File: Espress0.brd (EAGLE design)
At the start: 36.8 x 39.4 mm, 41 parts, among them CN1 4U#20329, Q2 reset, U1 AP2112K-3.3, U2 2MB Flash, U3 MCP73831T-2ACI/OT

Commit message: Add files via upload
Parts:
- moved PWR 0.38 mm to (29.7, 3.94)
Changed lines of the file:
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@@
 <text x="4.699" y="27.305" size="0.6096" layer="121" font="vector" rot="R90">SDA</text>
 <text x="7.239" y="25.019" size="0.6096" layer="121" font="vector">SCL</text>
-<text x="6.35" y="35.56" size="1.6764" layer="121" font="fixed">Espress0</text>
+<text x="6.223" y="35.179" size="1.6764" layer="121" font="fixed">Espress0</text>
 <text x="30.48" y="36.195" size="0.6096" layer="122" rot="MR0">Based on Trinket m0 by Adafruit Industries.</text>
-<text x="6.35" y="33.782" size="0.6096" layer="121">04/2018 - v0.2</text>
+<text x="31.496" y="1.143" size="0.6096" layer="122" rot="MR0">04/2018 - v0.2</text>
 <text x="5.08" y="1.016" size="0.6096" layer="121">www.timothygarcia.ca</text>
 <text x="1.016" y="25.908" size="0.6096" layer="121" font="vector" rot="R90">pa05</text>
@@
 <text x="35.56" y="31.75" size="0.6096" layer="121" font="vector" rot="R270">VBAT</text>
 <text x="35.56" y="28.702" size="0.6096" layer="121" font="vector" rot="R270">GND</text>
-<text x="30.48" y="36.195" size="0.6096" layer="121" rot="R180">a trinket m0 haxpress board</text>
+<text x="30.48" y="36.068" size="0.6096" layer="121" rot="R180">a trinket m0 haxpress board</text>
 <text x="30.48" y="37.592" size="0.6096" layer="122" rot="MR0.6">Designed for CircuitPython</text>
 <text x="30.48" y="34.798" size="0.6096" layer="122" rot="MR0">Open Source Hardware</text>
@@
 <attribute name="NAME" x="20.858" y="32.242" size="0.4064" layer="25" ratio="18"/>
 </element>
-<element name="PWR" library="microbuilder" package="CHIPLED_0603_NOOUTLINE" value="green" x="29.337" y="3.937" smashed="yes" rot="R180">
-<attribute name="NAME" x="28.702" y="1.524" size="0.8128" layer="25" ratio="18"/>
-<attribute name="VALUE" x="28.829" y="5.461" size="0.4064" layer="121" ratio="10"/>
+<element name="PWR" library="microbuilder" package="CHIPLED_0603_NOOUTLINE" value="green" x="29.718" y="3.937" smashed="yes" rot="R180">
+<attribute name="NAME" x="31.369" y="6.35" size="0.8128" layer="25" ratio="18" rot="R180"/>
+<attribute name="VALUE" x="28.702" y="2.667" size="0.4064" layer="121" ratio="10" rot="R90"/>
 </element>
 <element name="Q2" library="microbuilder" package="BTN_KMR2_4.6X2.8" value="reset" x="33.401" y="15.24" smashed="yes" rot="R270">
@@
 </element>
 <element name="R4" library="microbuilder" package="0603-NO" value="10K" x="27.305" y="3.81" smashed="yes" rot="R270">
-<attribute name="NAME" x="26.289" y="3.048" size="0.6096" layer="121" font="vector" ratio="18" rot="R180"/>
-<attribute name="VALUE" x="26.289" y="2.159" size="0.4064" layer="121" font="vector" ratio="10" rot="R180"/>
+<attribute name="NAME" x="25.781" y="3.302" size="0.6096" layer="121" font="vector" ratio="18" rot="R270"/>
+<attribute name="VALUE" x="27.686" y="5.969" size="0.4064" layer="121" font="vector" ratio="10" rot="R180"/>
 </element>
 <element name="R5" library="microbuilder" package="0603-NO" value="10K" x="7.62" y="15.24" smashed="yes" rot="R180">
@@
 </element>
 <element name="SWC" library="testpad" package="B1,27" value="TPB1,27" x="27.559" y="20.574" smashed="yes" rot="MR0">
-<attribute name="NAME" x="28.575" y="21.082" size="0.4064" layer="26" ratio="10" rot="MR180"/>
+<attribute name="NAME" x="28.321" y="21.463" size="0.4064" layer="26" ratio="10" rot="MR180"/>
 <attribute name="TP_SIGNAL_NAME" value="" x="28.194" y="18.669" size="1" layer="38" rot="MR0"/>
 <attribute name="VALUE" x="28.194" y="19.812" size="0.0254" layer="28" rot="MR0"/>
 </element>
 <element name="SWD" library="testpad" package="B1,27" value="TPB1,27" x="25.273" y="22.733" smashed="yes" rot="MR0">
-<attribute name="NAME" x="25.273" y="21.336" size="0.4064" layer="26" ratio="10" rot="MR180"/>
+<attribute name="NAME" x="24.765" y="24.511" size="0.4064" layer="26" ratio="10" rot="MR180"/>
 <attribute name="TP_SIGNAL_NAME" value="" x="25.908" y="20.828" size="1" layer="38" rot="MR0"/>
 <attribute name="VALUE" x="25.908" y="21.971" size="0.0254" layer="28" rot="MR0"/>
@@
 </element>
 <element name="U1" library="microbuilder" package="SOT23-5" value="AP2112K-3.3" x="27.559" y="17.018" smashed="yes" rot="R90">
-<attribute name="NAME" x="29.464" y="18.488" size="0.8128" layer="25" ratio="18" rot="R90"/>
-<attribute name="VALUE" x="29.845" y="19.612" size="0.4064" layer="121" ratio="10" rot="R270"/>
+<attribute name="NAME" x="28.775" y="18.796" size="0.6096" layer="25" ratio="18"/>
+<attribute name="VALUE" x="29.845" y="18.342" size="0.3048" layer="121" ratio="10" rot="R270"/>
 </element>
 <element name="U2" library="microbuilder" package="SOIC8_208MIL" value="2MB Flash" x="11.049" y="10.16" smashed="yes" rot="R90">
@@
 <wire x1="29.4350875" y1="19.891" x2="30.548" y2="19.891" width="0.3048" layer="1"/>
 <wire x1="27.81315" y1="20.32" x2="29.0060875" y2="20.32" width="0.3048" layer="1"/>
-<wire x1="31.389" y1="19.05" x2="31.389" y2="9.799" width="0.3048" layer="1"/>
+<wire x1="31.389" y1="19.05" x2="31.389" y2="12.7" width="0.3048" layer="1"/>
+<wire x1="31.389" y1="12.7" x2="31.389" y2="9.799" width="0.3048" layer="1"/>
 <wire x1="31.389" y1="9.799" x2="30.48" y2="8.89" width="0.3048" layer="1"/>
 <wire x1="30.48" y1="8.89" x2="26.67" y2="8.89" width="0.3048" layer="1"/>
@@
 <wire x1="30.353" y1="28.736" x2="30.353" y2="29.845" width="0.3048" layer="1"/>
 <wire x1="30.353" y1="29.845" x2="30.607" y2="30.099" width="0.3048" layer="1"/>
-<wire x1="21.844" y1="6.985" x2="24.384" y2="6.985" width="0.4064" layer="1"/>
+<wire x1="21.844" y1="6.985" x2="22.86" y2="6.985" width="0.4064" layer="1"/>
+<wire x1="22.86" y1="6.985" x2="24.384" y2="6.985" width="0.4064" layer="1"/>
 <wire x1="25.146" y1="7.747" x2="25.146" y2="10.922" width="0.4064" layer="1"/>
 <wire x1="24.384" y1="6.985" x2="25.146" y2="7.747" width="0.4064" layer="1"/>
@@
 <contactref element="R4" pad="1"/>
 <contactref element="PWR" pad="A"/>
-<wire x1="29.337" y1="4.687" x2="27.332" y2="4.687" width="0.3048" layer="1"/>
+<wire x1="29.718" y1="4.687" x2="27.332" y2="4.687" width="0.3048" layer="1"/>
 <wire x1="27.332" y1="4.687" x2="27.305" y2="4.66" width="0.3048" layer="1"/>
 </signal>
@@
 <wire x1="33.3558" y1="12.61375" x2="33.02" y2="12.27795" width="0.3048" layer="1"/>
 <wire x1="31.8462" y1="15.27585" x2="33.3558" y2="13.76625" width="0.3048" layer="1"/>
-<wire x1="31.8462" y1="27.8312" x2="31.8462" y2="15.27585" width="0.3048" layer="1"/>
+<wire x1="31.8462" y1="27.8312" x2="31.8462" y2="21.59" width="0.3048" layer="1"/>
+<wire x1="31.8462" y1="21.59" x2="31.8462" y2="15.27585" width="0.3048" layer="1"/>
 <wire x1="31.8462" y1="27.8312" x2="29.62675" y2="27.8312" width="0.3048" layer="1"/>
 <wire x1="27.8431" y1="25.08" x2="28.636" y2="25.08" width="0.3048" layer="1"/>
@@
 <contactref element="U1" pad="3"/>
 <wire x1="28.4345" y1="10.922" x2="29.7315" y2="10.922" width="0.4064" layer="1"/>
-<wire x1="29.7315" y1="10.922" x2="29.7315" y2="13.7955" width="0.4064" layer="1"/>
+<wire x1="29.7315" y1="10.922" x2="29.7315" y2="12.7" width="0.4064" layer="1"/>
+<wire x1="29.7315" y1="12.7" x2="29.7315" y2="13.7955" width="0.4064" layer="1"/>
 <wire x1="29.7315" y1="13.7955" x2="29.779" y2="13.843" width="0.4064" layer="1"/>
 <wire x1="28.11180625" y1="16.3874" x2="27.9035" y2="16.59570625" width="0.4064" layer="1"/>
@@
 <wire x1="23.749" y1="8.128" x2="25.781" y2="6.096" width="0.3048" layer="16"/>
 <wire x1="6.35" y1="15.24" x2="6.77" y2="15.24" width="0.4064" layer="1"/>
-<wire x1="24.384" y1="16.168" x2="26.1589" y2="16.168" width="0.4064" layer="1"/>
+<wire x1="24.384" y1="16.168" x2="25.4" y2="16.168" width="0.4064" layer="1"/>
+<wire x1="25.4" y1="16.168" x2="26.1589" y2="16.168" width="0.4064" layer="1"/>
 <wire x1="26.1589" y1="16.168" x2="26.2589" y2="16.068" width="0.4064" layer="1"/>
 <via x="10.922" y="18.288" extent="1-16" drill="0.35"/>

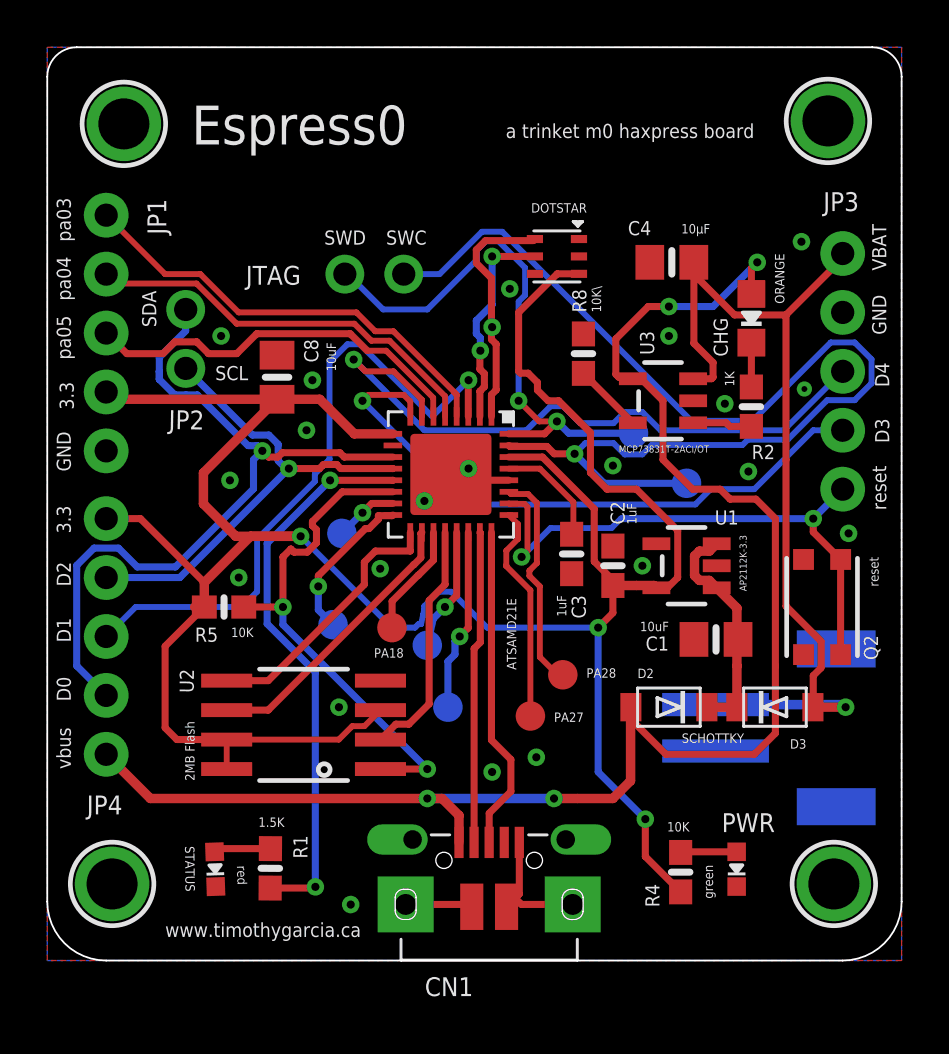
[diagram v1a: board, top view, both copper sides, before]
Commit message: v0.3
* Layout adjusted and schematic updated, pin header arrangement no longer matches 1:1 with a Trinket m0 board
* Trace diameter for power lines adjusted for 20mm, data for 15mm
* Removed "antennas", trapped copper that is grounded
* Issues re: "Crosstalk" lines were adjusted to have more space and or GND between lines.
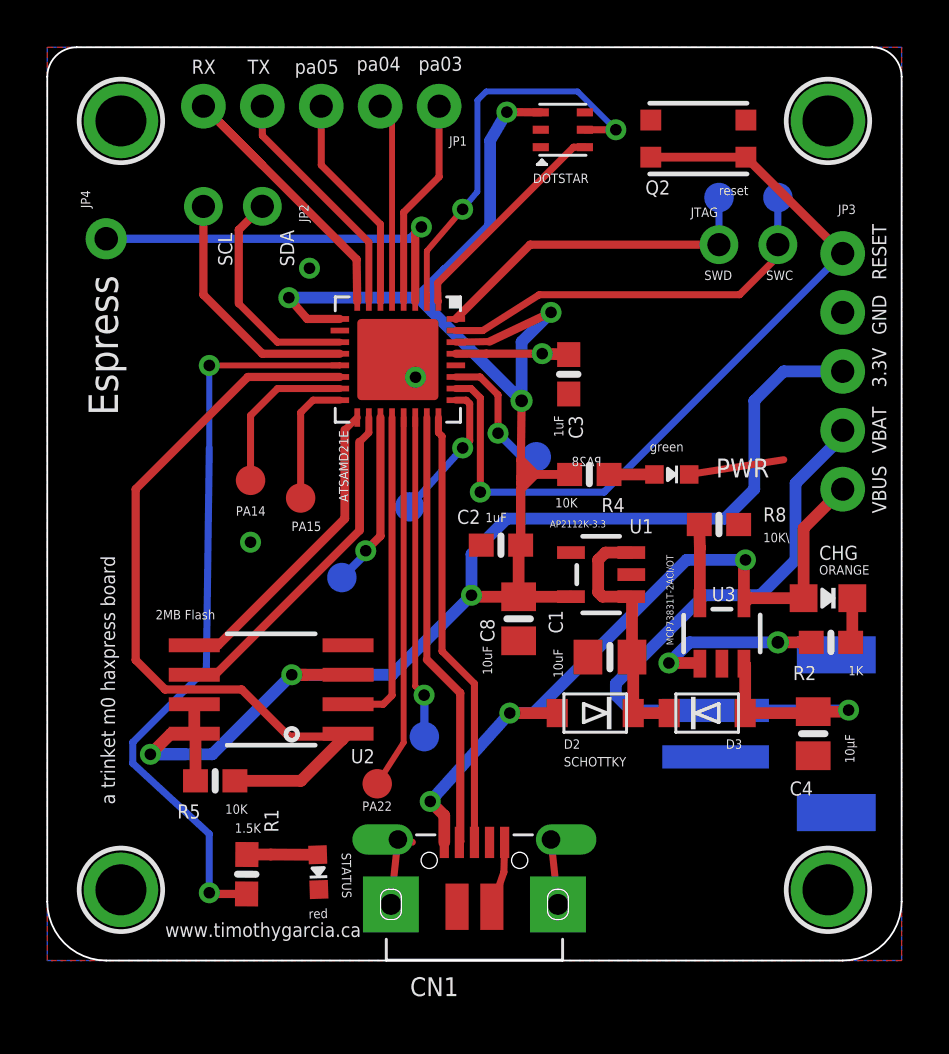
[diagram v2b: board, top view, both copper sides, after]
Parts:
- JP4: device microbuilder:1X05_ROUND_76 -> adafruit:1X01-CLEANBIG
- moved C4 21.2 mm to (33.0, 9.78), turned to 270 degrees
- moved Q2 20.9 mm to (28.1, 35.4), turned to 180 degrees
- moved R4 17.6 mm to (23.4, 21.0), turned to 180 degrees
- moved PWR 17.2 mm to (26.9, 21.0), turned to 270 degrees
- moved JP4 17.1 mm to (2.54, 31.1), turned to 90 degrees
- moved JTAG 16.2 mm to (30.2, 30.9)
- moved C8 14.7 mm to (20.3, 14.7), turned to 270 degrees
- moved JP1 13.5 mm to (11.8, 36.8), turned to 180 degrees
- moved SWC 12.9 mm to (31.5, 32.9)
- moved CHG 12.5 mm to (33.7, 15.6), turned to 270 degrees
- moved SWD 10.8 mm to (29.0, 32.9)
- moved R2 10.7 mm to (33.8, 13.7), turned to 180 degrees
- moved PA27 10.4 mm to (15.6, 19.6), flipped to the bottom, turned to 270 degrees
- moved U3 10.3 mm to (29.1, 14.1), turned to 0 degrees
- moved PA28 9.47 mm to (21.1, 21.7), flipped to the bottom, turned to 180 degrees
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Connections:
- net !RESET: now also JP3.1; no longer JP3.5
- net 3.3V: now also JP3.3; no longer JP1.4, JP4.1
- net D0_A4_PA08_SDA: no longer JP4.4
- net D1_A0_PA02: now also JP4.1; no longer JP4.3
- net D2_A1_PA09_SCL_MISO: no longer JP4.2
- net D3_A3_PA07_RXD_SCK: now also JP1.5; no longer JP3.4
- net D4_A2_PA06_TXD_MOSI: now also JP1.4; no longer JP3.3
- net GND: no longer JP1.5
- net VBAT: now also JP3.4; no longer JP3.1
- net VBUS: now also JP3.5; no longer JP4.5
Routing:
- net VBUS: track 68.6 -> 32.0 mm, vias 4 -> 3
- net SWC: track 50.2 -> 17.6 mm, vias 1 -> 0
- net D0_A4_PA08_SDA: track 33.0 -> 9.66 mm, vias 1 -> 0
- net D4_A2_PA06_TXD_MOSI: track 29.0 -> 10.3 mm, vias 1 -> 0
- net D3_A3_PA07_RXD_SCK: track 26.8 -> 14.7 mm, vias 1 -> 0
- net PA14_FLASHCS: track 22.2 -> 34.2 mm, vias 2 -> 0
- net D1_A0_PA02: track 28.3 -> 17.1 mm
- net N$7: track 5.31 -> 16.1 mm, vias 1 -> 0
- net !RESET: track 24.5 -> 35.2 mm, vias 2 -> 1
- net 3.3V: track 113.8 -> 103.2 mm, vias 3 -> 7
- net D2_A1_PA09_SCL_MISO: track 21.1 -> 10.7 mm, vias 1 -> 0
- net PA03: track 19.3 -> 9.05 mm
- net SWD: track 24.0 -> 14.7 mm, vias 2 -> 0
- net PA04: track 17.7 -> 8.63 mm
- net N$2: track 24.2 -> 32.8 mm
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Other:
- board text added: "04/2018 - v0.3"
- board text added: "3.3V"
- board text added: "Designed for CircuitPython, but works with Arduino too!"
- board text added: "Espress"
- board text added: "RESET"
- board text added: "RX"
- board text added: "TX"
- board text added: "VBUS"
- board text removed: "04/2018 - v0.2"
- board text removed: "3.3"
- board text removed: "D0"
- board text removed: "D1"
- board text removed: "D2"
- board text removed: "Designed for CircuitPython"
- board text removed: "Espress0"
- board text removed: "reset"
- board text removed: "vbus"

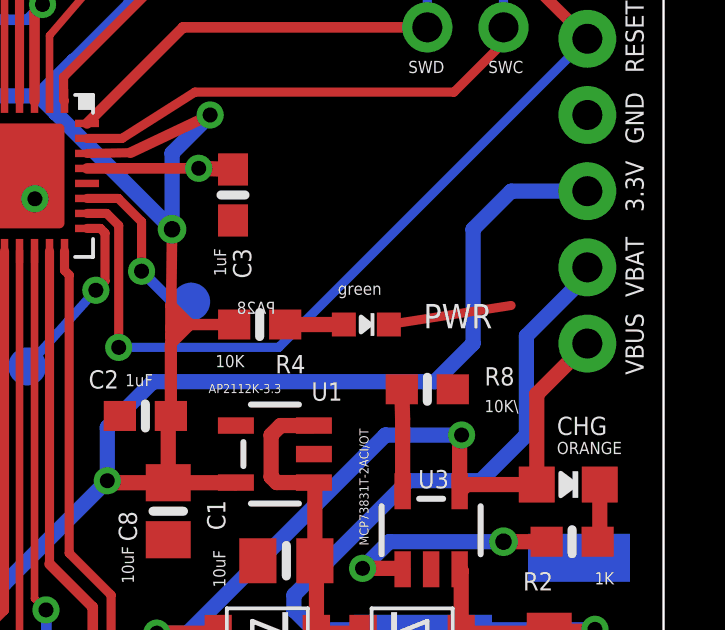
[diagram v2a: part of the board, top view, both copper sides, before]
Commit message: Add files via upload
Stray trace removed
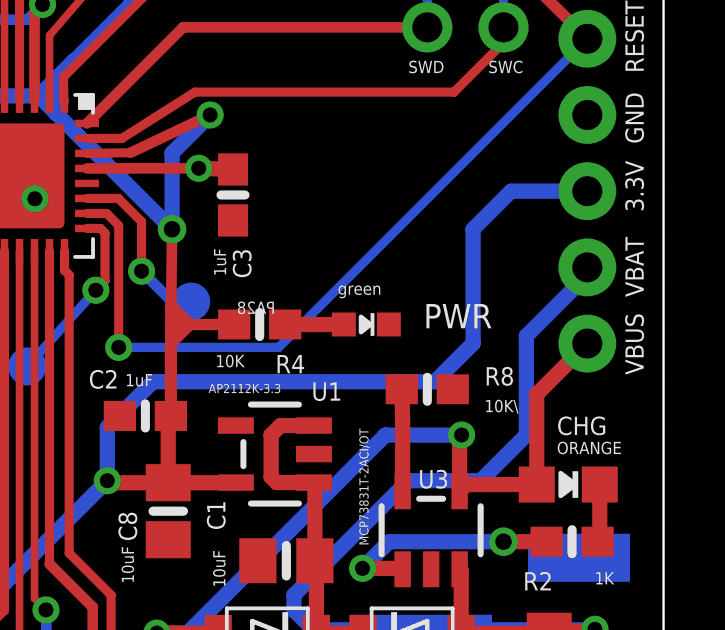
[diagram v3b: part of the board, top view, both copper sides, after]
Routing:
- net GND: track 14.3 -> 10.2 mm
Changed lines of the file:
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@@
 <wire x1="15.113" y1="25.908" x2="15.875" y2="25.146" width="0.508" layer="1"/>
 <via x="11.303" y="29.845" extent="1-16" drill="0.5"/>
-<wire x1="27.674" y1="20.955" x2="31.75" y2="21.59" width="0.3048" layer="1"/>
 </signal>
 <signal name="D+">

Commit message: Add files via upload
Removed a wiggle
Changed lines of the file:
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@@
 <wire x1="15.113" y1="25.908" x2="15.875" y2="25.146" width="0.508" layer="1"/>
 <via x="11.303" y="29.845" extent="1-16" drill="0.5"/>
+<wire x1="18.708" y1="17.907" x2="20.32" y2="13.782" width="0" layer="19" extent="1-1"/>
 </signal>
 <signal name="D+">
 <contactref element="CN1" pad="D+"/>
 <contactref element="ATSAMD21E" pad="24"/>
-<wire x1="16.863" y1="23.408" x2="16.863" y2="22.761" width="0.3048" layer="1"/>
-<wire x1="16.863" y1="22.761" x2="17.018" y2="22.606" width="0.3048" layer="1"/>
-<wire x1="17.018" y1="13.335" x2="18.415" y2="11.938" width="0.3048" layer="1"/>
+<wire x1="17.399" y1="12.954" x2="18.415" y2="11.938" width="0.3048" layer="1"/>
 <wire x1="18.415" y1="11.938" x2="18.415" y2="5.093" width="0.3048" layer="1"/>
-<wire x1="17.018" y1="22.606" x2="17.018" y2="13.335" width="0.3048" layer="1"/>
+<wire x1="16.863" y1="23.408" x2="16.863" y2="19.84" width="0.3048" layer="1"/>
+<wire x1="16.863" y1="19.84" x2="17.399" y2="19.05" width="0.3048" layer="1"/>
+<wire x1="17.399" y1="19.05" x2="17.399" y2="12.954" width="0.3048" layer="1"/>
 </signal>
 <signal name="D-">

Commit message: Add files via upload
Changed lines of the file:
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@@
 <wire x1="15.113" y1="25.908" x2="15.875" y2="25.146" width="0.508" layer="1"/>
 <via x="11.303" y="29.845" extent="1-16" drill="0.5"/>
-<wire x1="18.708" y1="17.907" x2="20.32" y2="13.782" width="0" layer="19" extent="1-1"/>
 </signal>
 <signal name="D+">
@@
 <wire x1="17.399" y1="12.954" x2="18.415" y2="11.938" width="0.3048" layer="1"/>
 <wire x1="18.415" y1="11.938" x2="18.415" y2="5.093" width="0.3048" layer="1"/>
-<wire x1="16.863" y1="23.408" x2="16.863" y2="19.84" width="0.3048" layer="1"/>
-<wire x1="16.863" y1="19.84" x2="17.399" y2="19.05" width="0.3048" layer="1"/>
-<wire x1="17.399" y1="19.05" x2="17.399" y2="12.954" width="0.3048" layer="1"/>
+<wire x1="16.863" y1="23.408" x2="16.863" y2="21.59" width="0.3048" layer="1"/>
+<wire x1="16.863" y1="21.59" x2="16.863" y2="21.11" width="0.3048" layer="1"/>
+<wire x1="16.863" y1="21.11" x2="16.863" y2="15.268" width="0.3048" layer="1"/>
+<wire x1="16.863" y1="15.268" x2="17.399" y2="14.732" width="0.3048" layer="1"/>
+<wire x1="17.399" y1="14.732" x2="17.399" y2="12.954" width="0.3048" layer="1"/>
 </signal>
 <signal name="D-">

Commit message: Add files via upload
* Adjusted traces on VBAT, pa04, SDA, 3.3V lines on SPI flash and CS pin remap USB GND
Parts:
- moved STATUS 1.27 mm to (10.4, 3.81), turned to 180 degrees
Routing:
- net PA14_FLASHCS: track 34.2 -> 39.6 mm
- net VBAT: track 34.5 -> 32.3 mm
- net N$1: track 3.05 -> 1.81 mm
- net 3.3V: track 103.2 -> 104.4 mm, vias 7 -> 6
- net GND: track 10.2 -> 9.04 mm
- net A3: track 9.58 -> 10.2 mm
- net D0_A4_PA08_SDA: track 9.66 -> 9.10 mm
